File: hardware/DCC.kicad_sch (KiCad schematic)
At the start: 10 parts, among them U3 6N137, U301 AMS1117-5.0

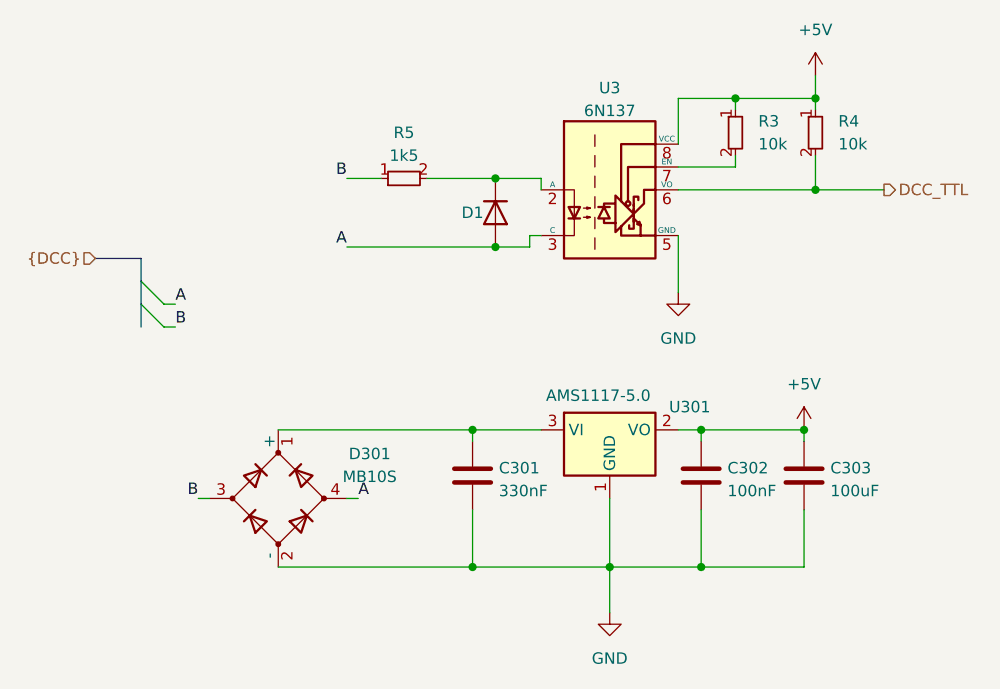
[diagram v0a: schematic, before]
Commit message: organized board files and added pictures
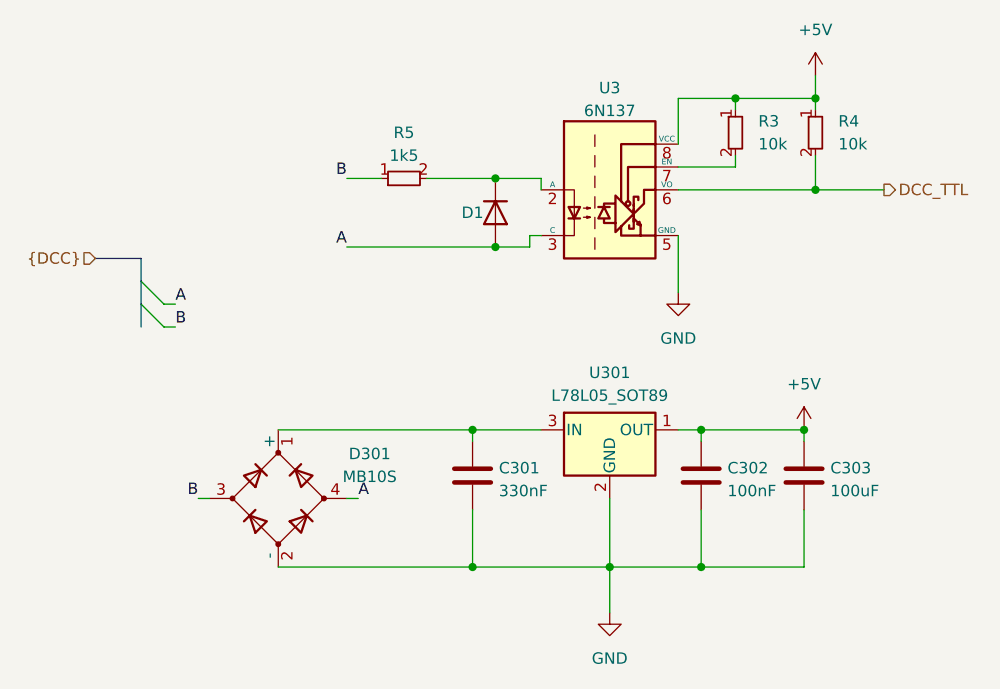
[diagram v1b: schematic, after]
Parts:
- removed U301: AMS1117-5.0, Package_TO_SOT_SMD:SOT-223-3_TabPin2, symbol custom_kicad_lib_sk:AMS1117-5.0
- added U301: L78L05_SOT89, Package_TO_SOT_SMD:SOT-89-3, symbol Regulator_Linear:L78L05_SOT89
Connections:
- net +5V: now also U301.1 (OUT)
- net GND: now also U301.2 (GND)
- net at C301.1, D301.1 (+): now also U301.3 (IN)
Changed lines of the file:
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@@
+	)
+	(symbol
+		(lib_id "Regulator_Linear:L78L05_SOT89")
+		(at 128.27 123.19 0)
+		(unit 1)
+		(exclude_from_sim no)
+		(in_bom yes)
+		(on_board yes)
+		(dnp no)
+		(fields_autoplaced yes)
+		(property "Reference" "U301"
+			(at 128.27 116.84 0)
+			(effects
+				(font
+					(size 1.27 1.27)
+				)
+			)
+		)
+		(property "Value" "L78L05_SOT89"
+			(at 128.27 119.38 0)
+			(effects
+				(font
+					(size 1.27 1.27)
+				)
+			)
+		)
+		(property "Footprint" "Package_TO_SOT_SMD:SOT-89-3"
+			(at 128.27 118.11 0)
+			(effects
+				(font
+					(size 1.27 1.27)
+					(italic yes)
+				)
+				(hide yes)
+			)
+		)
+		(property "Datasheet" "http://www.st.com/content/ccc/resource/technical/document/datasheet/15/55/e5/aa/23/5b/43/fd/CD00000446.pdf/files/CD00000446.pdf/jcr:content/translations/en.CD00000446.pdf"
+			(at 128.27 124.46 0)
+			(effects
+				(font
+					(size 1.27 1.27)
+				)
+				(hide yes)
+			)
+		)
+		(property "Description" "Positive 100mA 30V Linear Regulator, Fixed Output 5V, SOT-89"
+			(at 128.27 123.19 0)
+			(effects
+				(font
+					(size 1.27 1.27)
+				)
+				(hide yes)
+			)
+		)
+		(property "JLCPCB Part#" "C42738"
+			(at 128.27 123.19 0)
+			(effects
+				(font
+					(size 1.27 1.27)
+				)
+				(hide yes)
+			)
+		)
+		(pin "2"
+		)
+		(pin "1"
+		)
+		(pin "3"
+		)
+		(instances
+			(project ""
+				(path "/5ccbe098-5784-427e-9721-db3f20de1ebf/8844a919-370c-43dd-897a-ce1fcbceebfa"
+					(reference "U301")
+					(unit 1)
+				)
+			)
+		)
 	)
 	(symbol
@@
 					(unit 1)
 				)
-			)
-		)
-	)
-	(symbol
-		(lib_id "custom_kicad_lib_sk:AMS1117-5.0")
-		(at 128.27 123.19 0)
-		(unit 1)
-		(exclude_from_sim no)
-		(in_bom yes)
-		(on_board yes)
-		(dnp no)
-		(property "Reference" "U301"
-			(at 137.16 120.65 0)
-			(effects
-				(font
-					(size 1.27 1.27)
-				)
-			)
-		)
-		(property "Value" "AMS1117-5.0"
-			(at 127 119.38 0)
-			(effects
-				(font
-					(size 1.27 1.27)
-				)
-			)
-		)
-		(property "Footprint" "Package_TO_SOT_SMD:SOT-223-3_TabPin2"
-			(at 128.27 118.11 0)
-			(effects
-				(font
-					(size 1.27 1.27)
-				)
-				(hide yes)
-			)
-		)
-		(property "Datasheet" "http://www.advanced-monolithic.com/pdf/ds1117.pdf"
-			(at 130.81 129.54 0)
-			(effects
-				(font
-					(size 1.27 1.27)
-				)
-				(hide yes)
-			)
-		)
-		(property "Description" "1A Low Dropout regulator, positive, 5.0V fixed output, SOT-223"
-			(at 128.27 123.19 0)
-			(effects
-				(font
-					(size 1.27 1.27)
-				)
-				(hide yes)
-			)
-		)
-		(property "JLCPCB Part#" "C6187"
-			(at 128.27 123.19 0)
-			(effects
-				(font
-					(size 1.27 1.27)
-				)
-				(hide yes)
-			)
-		)
-		(pin "1"
-		)
-		(pin "3"
-		)
-		(pin "2"
-		)
-		(instances
-			(project "solenoidDecoder"
-				(path "/5ccbe098-5784-427e-9721-db3f20de1ebf/8844a919-370c-43dd-897a-ce1fcbceebfa"
-					(reference "U301")
-					(unit 1)
-				)
